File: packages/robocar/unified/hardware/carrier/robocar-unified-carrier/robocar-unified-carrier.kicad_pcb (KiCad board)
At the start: 2 copper layers, 100 x 100 mm, 43 parts, among them J1 IDC 2x7 head cable, J10 Piezo, J11 Test: 3V3 5V GND VBAT, J12 Test: GND SDA SCL RST, J13 GND post, J14 GND post, J15 UART0 TX tap, J2 IDC 2x7 head cable, J3 XT30 pack in, J4 LM2596 module, J5 Motor left, J6 Motor right, J7 RCWL-1601 front, J8 RCWL-1601 rear, J9 SSD1306 0.91in, U1 XIAO ESP32-S3 Sense, U2 AMS1117-3.3

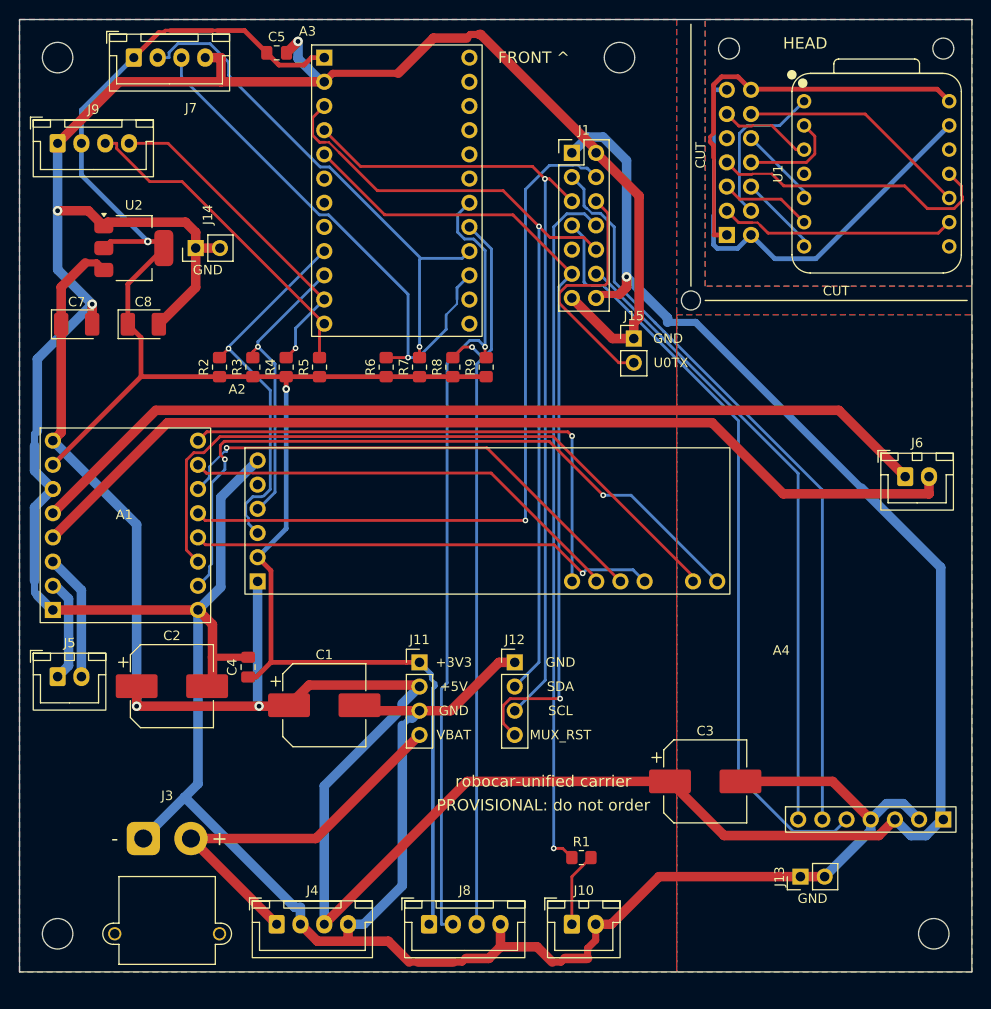
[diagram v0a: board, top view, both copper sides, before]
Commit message: feat(robocar-unified): rectangular main board with three head variants (#800)
* feat(kicad): spare head boards on a carrier cable

Lauri wants three head variants on one panel to try in the pan-tilt
cradle. A [[cables]] entry may now list spare_heads, each an mcu_ref and
a head_ref. The netlist gives every spare head its own copy of the MCU
socket and of the head connector, joined by HEAD2_*, HEAD3_* nets with
the same split as HEAD_*: the main board keeps one end, so the spare
heads stay off its nets. head_no_connect and the power-pad-on-a-rail rule
apply to each MCU copy.

The join rejects a malformed spare_heads entry and any spare ref that
repeats another ref. The balancebot netlist is unchanged (its #749
export test still passes byte for byte).

Co-Authored-By: Claude Opus 5.5 <noreply@anthropic.com>
Claude-Session: https://claude.ai/code/session_01LmLtwHDbHDLXFMLxCn3smf

* feat(parts): 2.0 mm head ribbon and a 12 mm board-mount buzzer

The head ribbon moves to a 2.0 mm 2x7 pin header at both ends, mated by a
2.0 mm IDC plug on 1.0 mm-pitch ribbon (Lauri, 2026-10-16). The cradle's
sides carry clips, so the header must sit at the head's top or bottom
edge; at 2.0 mm the 2x7 is 14 x 4 mm and fits across that edge beside the
XIAO, where the 17.8 mm 2.54 mm header does not. The reversal-safe pinout
is unchanged, and the KiCad 2.00 mm footprint numbers odd/even across its
rows like the 2.54 mm one, so a rotated plug still maps pin n to 15 - n.

piezo-buzzer-12mm is Lauri's buzzer: 12 mm, 7.6 mm pin pitch, soldered
to the board. Device:Buzzer names pin 1 "+" and Buzzer_12x9.5RM7.6 prints
"+" beside pad 1, which the registry's polarity tripwire checks.

The vendored subset drops the unused 2.54 mm 2x7 header and adds the two
new footprints.

Co-Authored-By: Claude Opus 5.5 <noreply@anthropic.com>
Claude-Session: https://claude.ai/code/session_01LmLtwHDbHDLXFMLxCn3smf

* docs(rcwl-1601): record the bench-verified pin order

Lauri verified the RCWL-1601 header order, VC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
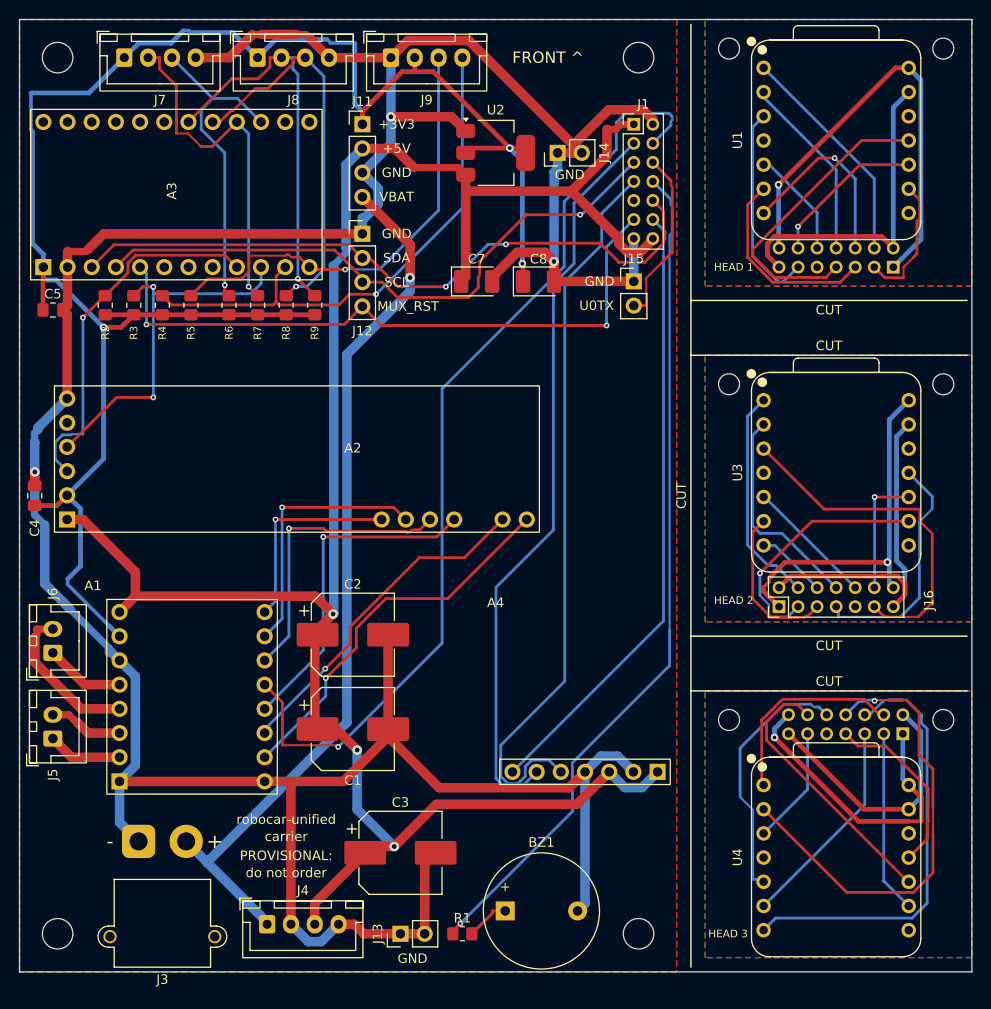
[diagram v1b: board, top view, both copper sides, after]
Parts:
- removed J10: Piezo, Connector_JST:JST_XH_B2B-XH-A_1x02_P2.50mm_Vertical
- added BZ1: Buzzer 12mm, Buzzer_Beeper:Buzzer_12x9.5RM7.6, F.Cu at (151.0, 193.6)
- added H10: M2, MountingHole:MountingHole_2.2mm_M2_ISO7380, F.Cu at (197.0, 173.6)
- added H7: M2, MountingHole:MountingHole_2.2mm_M2_ISO7380, F.Cu at (174.5, 138.3)
- added H8: M2, MountingHole:MountingHole_2.2mm_M2_ISO7380, F.Cu at (197.0, 138.3)
- added H9: M2, MountingHole:MountingHole_2.2mm_M2_ISO7380, F.Cu at (174.5, 173.6)
- added J16: IDC 2x7 head cable, Connector_PinHeader_2.00mm:PinHeader_2x07_P2.00mm_Vertical, F.Cu at (179.8, 161.7)
- added J17: IDC 2x7 head cable, Connector_PinHeader_2.00mm:PinHeader_2x07_P2.00mm_Vertical, B.Cu at (192.8, 175.0)
- added U3: XIAO ESP32-S3 Sense, Seeed_XIAO:XIAO-ESP32-S3-Socket, F.Cu at (185.8, 147.6)
- added U4: XIAO ESP32-S3 Sense, Seeed_XIAO:XIAO-ESP32-S3-Socket, F.Cu at (185.8, 188.0)
- H5, H6: footprint MountingHole:MountingHole_2.2mm_M2 -> MountingHole:MountingHole_2.2mm_M2_ISO7380
- J1, J2: footprint Connector_PinHeader_2.54mm:PinHeader_2x07_P2.54mm_Vertical -> Connector_PinHeader_2.00mm:PinHeader_2x07_P2.00mm_Vertical
- moved J8 92.8 mm to (125.0, 104.0)
- moved J6 91.4 mm to (103.5, 166.5), turned to 90 degrees
- moved J11 56.8 mm to (136.0, 111.0)
- moved J12 47.8 mm to (136.0, 122.5)
- moved J13 42.4 mm to (140.0, 196.0)
- moved C7 42.2 mm to (148.0, 127.5)
- moved C8 41.7 mm to (154.5, 127.5)
- moved J14 39.3 mm to (156.5, 114.0)
- moved U2 39.3 mm to (150.0, 114.0)
- moved A3 36.8 mm to (102.5, 126.0), turned to 90 degrees
- moved J9 36.1 mm to (139.0, 104.0)
- moved C5 35.8 mm to (103.5, 130.5)
- moved C3 32.9 mm to (140.0, 187.5)
- moved H4 31.0 mm to (165.0, 196.0)
- moved A4 30.4 mm to (167.0, 179.0)
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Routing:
- net MOT_A01: track 96.9 -> 8.38 mm
- net MOT_A02: track 101.9 -> 16.2 mm
- net +5V: track 301.4 -> 219.0 mm
- net GND: track 428.9 -> 354.5 mm
- net VBAT: track 41.2 -> 93.0 mm, vias 0 -> 1
- net HEAD3_PIEZO: track 0.00 -> 48.6 mm, vias 0 -> 1
- net HEAD3_UART0_TX: track 0.00 -> 45.6 mm
- net CH4_SCL: track 84.2 -> 40.3 mm
- net HEAD2_+5V: track 0.00 -> 37.9 mm, vias 0 -> 1
- net CH4_SDA: track 78.9 -> 41.0 mm
- net HEAD2_GND: track 0.00 -> 37.5 mm
- net HEAD2_MUX_RST: track 0.00 -> 36.5 mm
- net BIN2: track 72.0 -> 35.5 mm, vias 0 -> 1
- net PWMB: track 74.6 -> 40.2 mm, vias 2 -> 1
- net PWMA: track 55.1 -> 21.3 mm
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- added copper zone on B.Cu, net HEAD2_GND
- added copper zone on F.Cu, net HEAD2_GND
- added copper zone on B.Cu, net HEAD3_GND
- added copper zone on F.Cu, net HEAD3_GND
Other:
- outline, holes or cut-outs redrawn
- board text added: "HEAD 1"
- board text added: "HEAD 2"
- board text added: "HEAD 3"
- board text added: "PROVISIONAL:"
- board text added: "carrier"
- board text added: "do not order"
- board text added: "robocar-unified"
- board text removed: "HEAD"
- board text removed: "PROVISIONAL: do not order"
- board text removed: "robocar-unified carrier"

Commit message: feat(robocar-unified): MCP23017 socket and GPIO mirror header on the carrier (#803)
* feat(kicad): socket footprints from listed pad positions

A breakout socket's pads come from the pad centres its board page records,
which are read from the vendor's board file. The CJMCU-2317 has no board
file, so its page has no centres to read; its column spacing is a bench
measurement. A [[socket]] table may now give `pad_xy`, each pad's [x, y] in
footprint pad order, in place of `pads`. The outline, courtyard, pad shape
and the inside-the-outline and listed-once checks are unchanged.

The breakout-sockets README also said the courtyard bounds only the pads;
it has covered the module outline since #794.

Co-Authored-By: Claude Opus 5.5 <noreply@anthropic.com>
Claude-Session: https://claude.ai/code/session_01LmLtwHDbHDLXFMLxCn3smf

* docs(boards): record Lauri's OLED pin-order and CJMCU-2317 geometry checks

Lauri checked both fitted modules on 2026-10-16. The 0.91" SSD1306's pin
order (GND, VCC, SCL, SDA) matches the photo read, so its page and the
ssd1306-091-cable entry's source now say so; its other checks stay open.

On the CJMCU-2317 the first-named signal of each double-column row is on
the inner hole, the outer column is one 2.54 mm pitch outside the inner,
and the single column is 15.24 mm from the inner, with 2.54 mm rows. The
page gives those positions, which the carrier socket is built from. The
outline is still an estimate from a photo, and the address, RESET and
pull-up checks stay open. The "no board = key" caveat stays: the layout
model still has no inner row.

Co-Authored-By: Claude Opus 5.5 <noreply@anthropic.com>
Claude-Session: https://claude.ai/code/session_01LmLtwHDbHDLXFMLxCn3smf

* feat(parts): CJMCU-2317 socket and its GPIO mirror header

The robocar carrier takes the MCP23017 module by all 30 holes, so it sits
firmly and every pin reaches copper. CJMCU_2317_Socket lists the hole
positions from Lauri's 2026-10-16 measurement (pad_xy) and the page's
estim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
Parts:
- added A5: CJMCU-2317, Breakout_Sockets:CJMCU_2317_Socket, F.Cu at (160.7, 132.7)
- added J18: GPIO A/B, Connector_PinHeader_2.54mm:PinHeader_2x10_P2.54mm_Vertical, F.Cu at (167.0, 132.7)
- added R10: 10k, Resistor_SMD:R_0805_2012Metric_Pad1.20x1.40mm_HandSolder, F.Cu at (134.4, 133.3)
- added R11: 10k, Resistor_SMD:R_0805_2012Metric_Pad1.20x1.40mm_HandSolder, F.Cu at (138.4, 133.3)
- moved J9 82.5 mm to (125.3, 185.4)
- moved J14 68.4 mm to (144.0, 181.2)
- moved U2 56.8 mm to (145.6, 170.6), turned to 90 degrees
- moved C8 50.3 mm to (145.6, 177.0)
- moved C7 36.0 mm to (145.6, 163.4)
- moved J15 27.7 mm to (153.0, 102.3)
- moved J1 27.5 mm to (137.5, 106.0), turned to 90 degrees
- moved J13 15.0 mm to (150.5, 185.3)
- moved C3 2.00 mm to (142.0, 187.5)
- moved J11 2.00 mm to (134.0, 111.0)
- moved J12 2.00 mm to (134.0, 122.5)
- moved A2 1.30 mm to (105.0, 153.8)
- moved C4 1.30 mm to (101.6, 151.3)
- moved A1 0.60 mm to (110.5, 180.6)
- moved C1 0.60 mm to (135.0, 175.1)
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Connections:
- A3 pad 13: unconnected-(A3-Pin_13-Pad13) -> CH2_SDA
- A3 pad 14: unconnected-(A3-Pin_14-Pad14) -> CH2_SCL
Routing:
- net CH2_SDA: track 0.00 -> 55.5 mm, vias 0 -> 1
- net +3V3: track 192.4 -> 245.0 mm, vias 3 -> 1
- net CH2_SCL: track 0.00 -> 38.4 mm, vias 0 -> 3
- net GND: track 354.5 -> 387.1 mm, vias 3 -> 2
- net CH1_SDA: track 56.2 -> 88.5 mm, vias 1 -> 2
- net CH1_SCL: track 48.1 -> 78.6 mm, vias 1 -> 3
- net PIEZO: track 89.4 -> 114.3 mm
- net HEAD2_I2S_BCLK: track 26.4 -> 45.9 mm
- net I2S_LRCLK: track 65.2 -> 82.6 mm, vias 0 -> 3
- net BIN2: track 35.5 -> 51.9 mm
- net PWMB: track 40.2 -> 53.3 mm
- net MUX_RST: track 68.5 -> 59.4 mm, vias 2 -> 0
- net EXP_INTB: track 0.00 -> 7.35 mm
- net EXP_GPB6: track 0.00 -> 7.35 mm
- net EXP_GPB2: track 0.00 -> 7.35 mm
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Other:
- board text added: "3V3"
- board text added: "A"
- board text added: "A0"
- board text added: "A1"
- board text added: "A2"
- board text added: "B"
- board text added: "B0 A0"
- board text added: "B1 A1"
- board text added: "B2 A2"
- board text added: "B3 A3"
- board text added: "B4 A4"
- board text added: "B5 A5"
- board text added: "B6 A6"
- board text added: "B7 A7"
- board text added: "CHIP SIDE UP"
- board text added: "INTB INTA"
- board text added: "LABELS FACE DOWN"
- board text added: "NC"
- board text added: "RST"
- board text added: "VCC"
- board text added: "VCC GND"
